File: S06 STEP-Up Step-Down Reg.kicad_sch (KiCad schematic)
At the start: 49 parts, among them Q16 IAUCN04S7L019, Q17 IAUCN04S7L028, Q18 CSD17304Q3, Q19 IAUCN04S7L019, U5 LM51772RHAR

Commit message: Add a PCAL9714 SPI I/O expander for the load-switch enables and faults
New sheet S08 with U11 (PCAL9714, HVQFN-24) on the shared CLOCK/MOSI/MISO
bus. J3.32, which was ENSBC, becomes its chip select nCSIO.

- P0_0-P0_2 drive ENDAQ, ENSBC and ENEXT. J3.34/J3.36 become MCU_ENDAQ
  and MCU_ENEXT, and each reaches its enable only through a DNP 0R link
  (R96-R98). R95 links nCSIO to the expander CS.
- P0_4-P0_6 read the U6/U7/U9 power-good signals, and P0_7 reads U5
  nFLT/nINT.
- REGEN stays a direct J3.12 signal.
- RESET is divided from +12V (R99 100K, R100 40.2K), so the expander
  stays in reset while the 12 V rail is off.
- Pull-ups on CS and INT (R93, R94) and decoupling (C58, C59).

The README gains the port map, the links and the board work. The board
still needs Update PCB from Schematic.

Co-Authored-By: Claude Opus 5.5 <noreply@anthropic.com>
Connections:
- net nFLT: now reaches R40.2, U5.11 (nFLT/nINT)
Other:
- note added: "U5 nFLT/nINT to the I/O expander (S08)"
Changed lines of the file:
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@@
 		)
 	)
+	(text "U5 nFLT/nINT to the I/O expander (S08)"
+		(exclude_from_sim no)
+		(at 266.7 223.52 0)
+		(effects
+			(font
+				(size 1.27 1.27)
+			)
+			(justify left top)
+		)
+	)
 	(text "C"
 		(exclude_from_sim no)
@@
 	(wire
 		(pts
+			(xy 271.78 228.6) (xy 284.48 228.6)
+		)
+		(stroke
+			(width 0)
+			(type default)
+		)
+	)
+	(wire
+		(pts
 			(xy 346.71 59.69) (xy 356.87 59.69)
 		)
@@
 		)
 	)
+	(label "nFLT"
+		(at 140.97 175.26 0)
+		(effects
+			(font
+				(size 1.27 1.27)
+			)
+			(justify left bottom)
+		)
+	)
 	(label "MODE"
 		(at 142.24 160.02 180)
@@
 		)
 	)
+	(label "nFLT"
+		(at 271.78 228.6 180)
+		(effects
+			(font
+				(size 1.27 1.27)
+			)
+			(justify right bottom)
+		)
+	)
 	(label "LDVR1"
 		(at 137.16 95.25 0)
@@
 		)
 	)
+	(hierarchical_label "nFLT"
+		(shape output)
+		(at 284.48 228.6 0)
+		(effects
+			(font
+				(size 1.27 1.27)
+			)
+			(justify left)
+		)
+	)

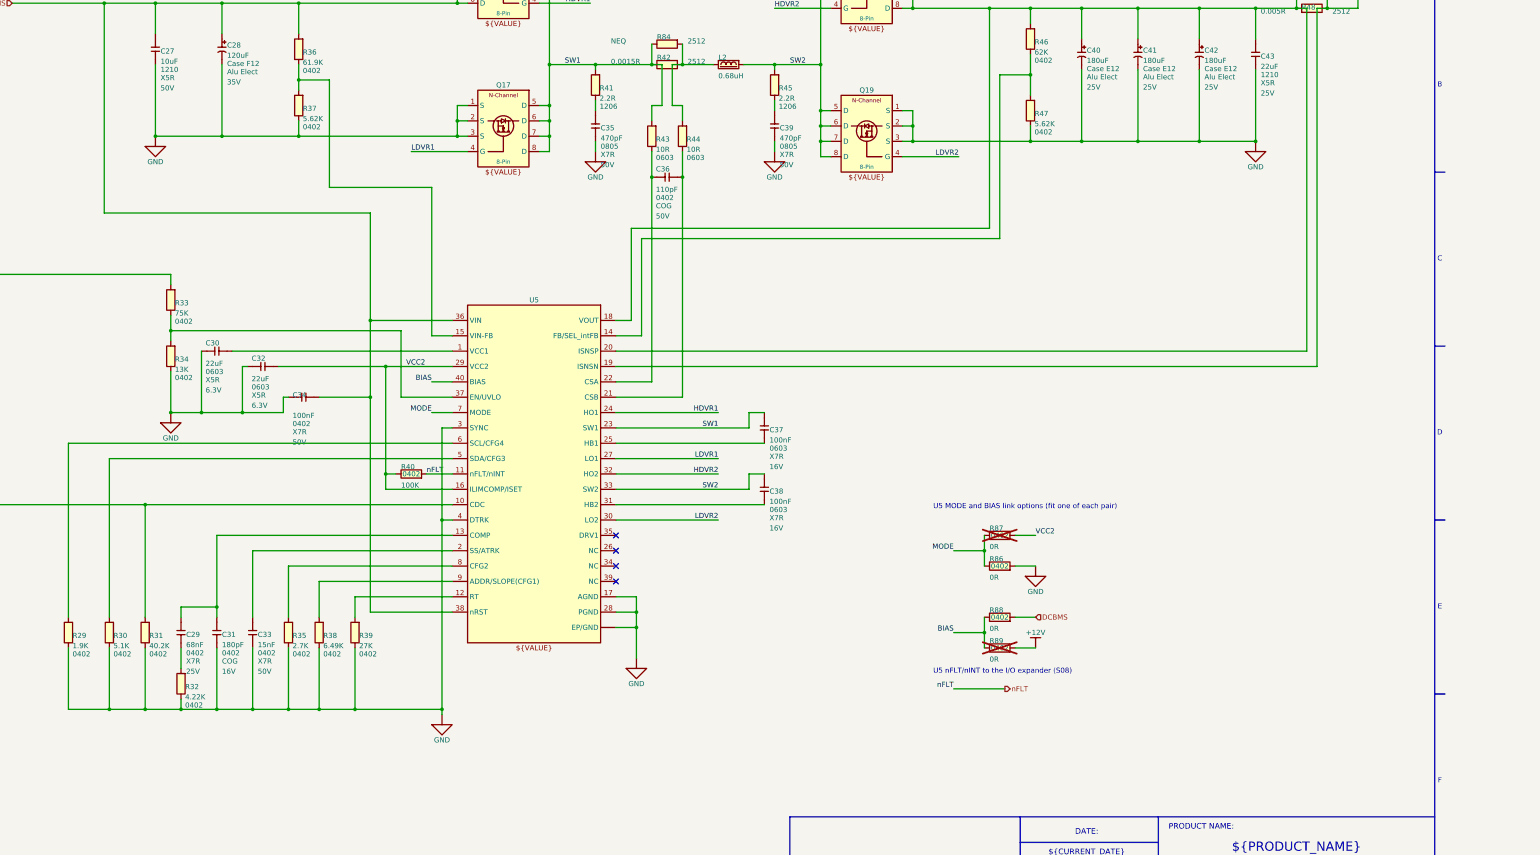
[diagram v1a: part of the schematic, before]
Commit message: BOM consolidation, OVLO divider to 1%, U5 fixes and I2C config option
- Consolidate passives: 1uF 50V to 0603, 100nF to 50V X7R 0402,
  10uF to 50V X7R 1210, 220nF to 0603, 10R to 0402 (100 -> 90 BOM lines)
- TPS22811 OVLO divider 1M/102K 0.1% -> 1M/100K 1% (12.6V min trip)
- U5 LM51772: C30 -> R102 10K to GND (VCC1 disabled), C32 -> 22uF 16V 0805,
  R29 1.9K -> 1.87K to sit inside the CFG4 window
- Add DNP I2C configuration option for U5 (R103-R107) on J3.34/J3.36,
  shared with R97/R98 fallback
- Document all changes in README.md

Co-Authored-By: Claude Opus 5.5 <noreply@anthropic.com>
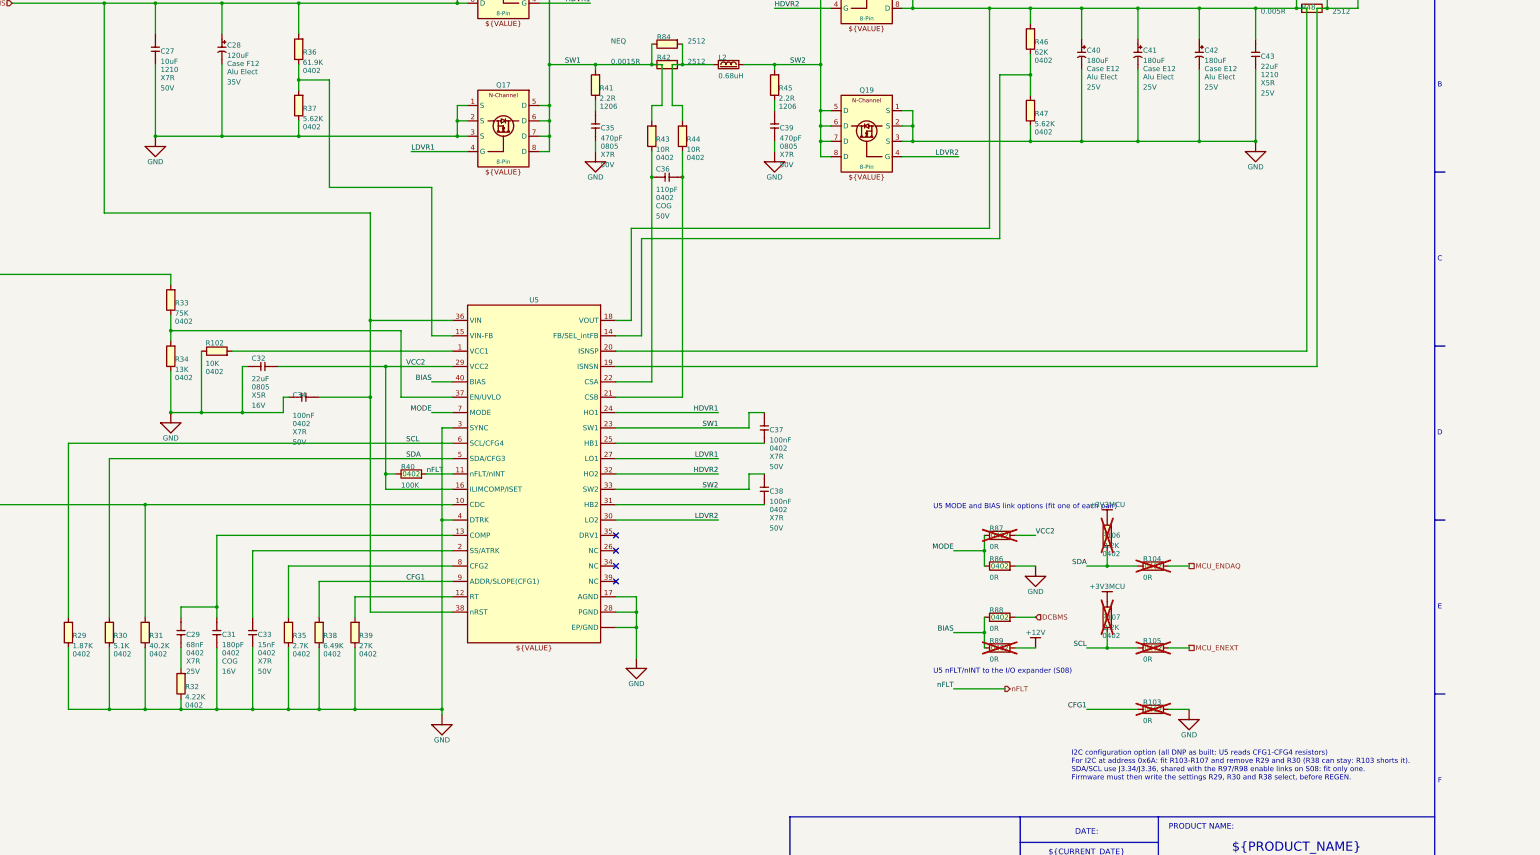
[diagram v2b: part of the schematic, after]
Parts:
- added R103, R104, R105: 0R, Resistor_SMD:R_0402_1005Metric, symbol Lattech Systems:Resistor 0R 0402
- added R106, R107: 2.2K, Resistor_SMD:R_0402_1005Metric, symbol Lattech Systems:Resistor 2.2K 1% 0402
- C27: symbol Lattech Systems:Capacitor 10uF 50V X5R 1210 -> Lattech Systems:Capacitor 10uF 50V X7R 1210; MANUFACTURER (none) -> Murata; MANUFACTURER_PN (none) -> GRM32ER71H106KA12L; MATERIAL X5R -> X7R; PL_SORT_GROUP (none) -> 2.3
- C32: footprint Capacitor_SMD:C_0603_1608Metric -> Capacitor_SMD:C_0805_2012Metric; symbol Lattech Systems:Capacitor 22uF 6.3V X5R 0603 -> Lattech Systems:Capacitor 22uF 16V X5R 0805; ALTIUM_FOOTPRINT 0603 -> 0805; MANUFACTURER ? -> Murata; MANUFACTURER_PN ? -> GRM21BR61C226ME44L; VOLTAGE 6.3V -> 16V
- C34: MANUFACTURER ? -> Yageo; MANUFACTURER_PN ? -> CC0402KPX7R9BB104
- C37, C38: footprint Capacitor_SMD:C_0603_1608Metric -> Capacitor_SMD:C_0402_1005Metric; symbol Lattech Systems:Capacitor 100nF 16V X7R 0603 -> Lattech Systems:Capacitor 100nF 50V X7R 0402; ALTIUM_FOOTPRINT 0603 -> 0402; MANUFACTURER (none) -> Yageo; MANUFACTURER_PN (none) -> CC0402KPX7R9BB104; PL_SORT_GROUP (none) -> 2.3; VOLTAGE 16V -> 50V
- R102: renamed from C30; value 22uF -> 10K; footprint Capacitor_SMD:C_0603_1608Metric -> Resistor_SMD:R_0402_1005Metric; symbol Lattech Systems:Capacitor 22uF 6.3V X5R 0603 -> Lattech Systems:Resistor 10K 1% 0402; ALTIUM_FOOTPRINT 0603 -> 0402; ALTIUM_VALUE 22uF -> 10K; MATERIAL X5R -> (none); VOLTAGE 6.3V -> (none)
- R29: value 1.9K -> 1.87K; symbol Lattech Systems:Resistor 1.9K 1% 0402 -> Lattech Systems:Resistor 1.87K 1% 0402; ALTIUM_VALUE 1.9K -> 1.87K
- R43, R44: footprint Resistor_SMD:R_0603_1608Metric -> Resistor_SMD:R_0402_1005Metric; symbol Lattech Systems:Resistor 10R 1% 0603 -> Lattech Systems:Resistor 10R 1% 0402; ALTIUM_FOOTPRINT 0603 -> 0402
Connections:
- net GND: now also R103.2
- net SDA: now reaches R30.2, U5.5 (SDA/CFG3)
- net SDA: now also R104.1, R106.1
- net SCL: now reaches R29.2, U5.6 (SCL/CFG4)
- net SCL: now also R105.1, R107.1
- net CFG1: now reaches R38.2, U5.9 (ADDR/SLOPE(CFG1))
- net CFG1: now also R103.1
- new net +3V3MCU: R106.2, R107.2
- new net MCU_ENDAQ: R104.2
- new net MCU_ENEXT: R105.2
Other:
- note added: "I2C configuration option (all DNP as built: U5 reads CFG1-CFG4 resistors) For I2C at address 0x6A: fit R103-R107 and remove R29 and R30 (R38 can stay: R103 shorts it). SDA/SCL use J3.34/J3.36, shared with the R97/R98 enable links on S08: fit only one. Firmware must then write the settings R29, R30 and R38 select, before REGEN."

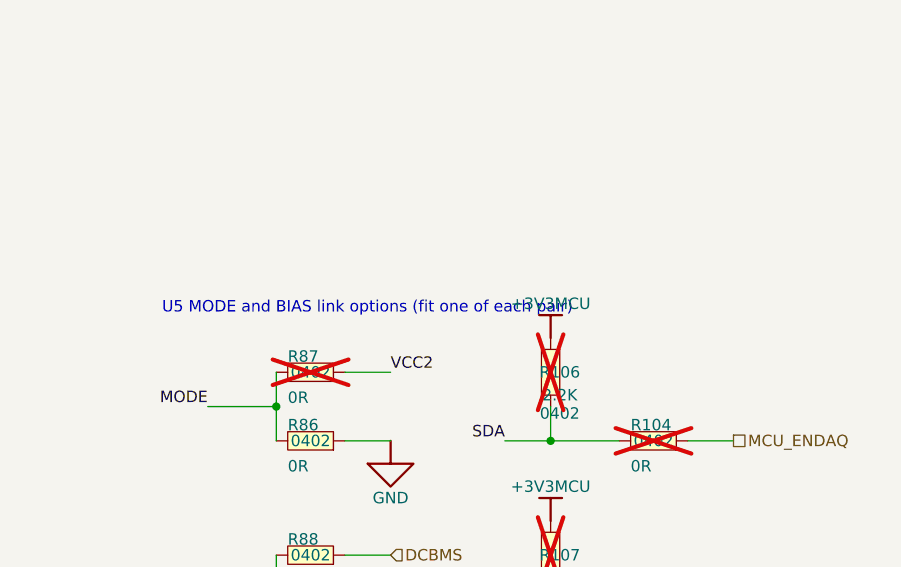
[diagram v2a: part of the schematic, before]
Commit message: Update the PCB from the schematic for the BOM consolidation
Brings in the footprint changes from 2fea505: C11-C14 and C24-C26 to
1210, C8/C9/C55 and C16 to 0603, C32 to 0805, C37/C38 and R43/R44 to
0402, C30 replaced by R102, and the U5 I2C option parts R103-R107.

Q20 moved clear of C42's courtyard, with a few other parts and a via
moved and zones refilled. Minimum hole clearance set to 0.182 mm.

The schematic changes are KiCad reordering items, plus one item moved
on S06.

Co-Authored-By: Claude Opus 5.5 <noreply@anthropic.com>
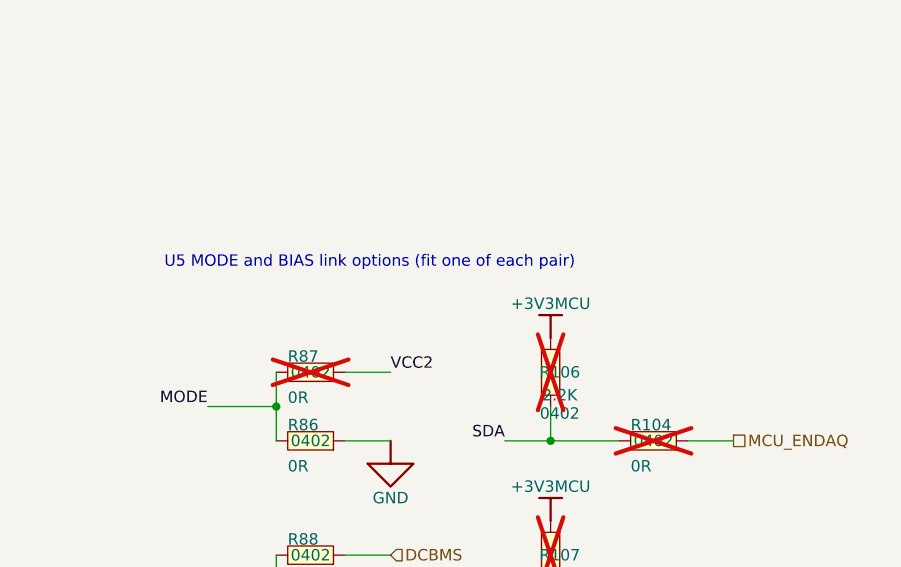
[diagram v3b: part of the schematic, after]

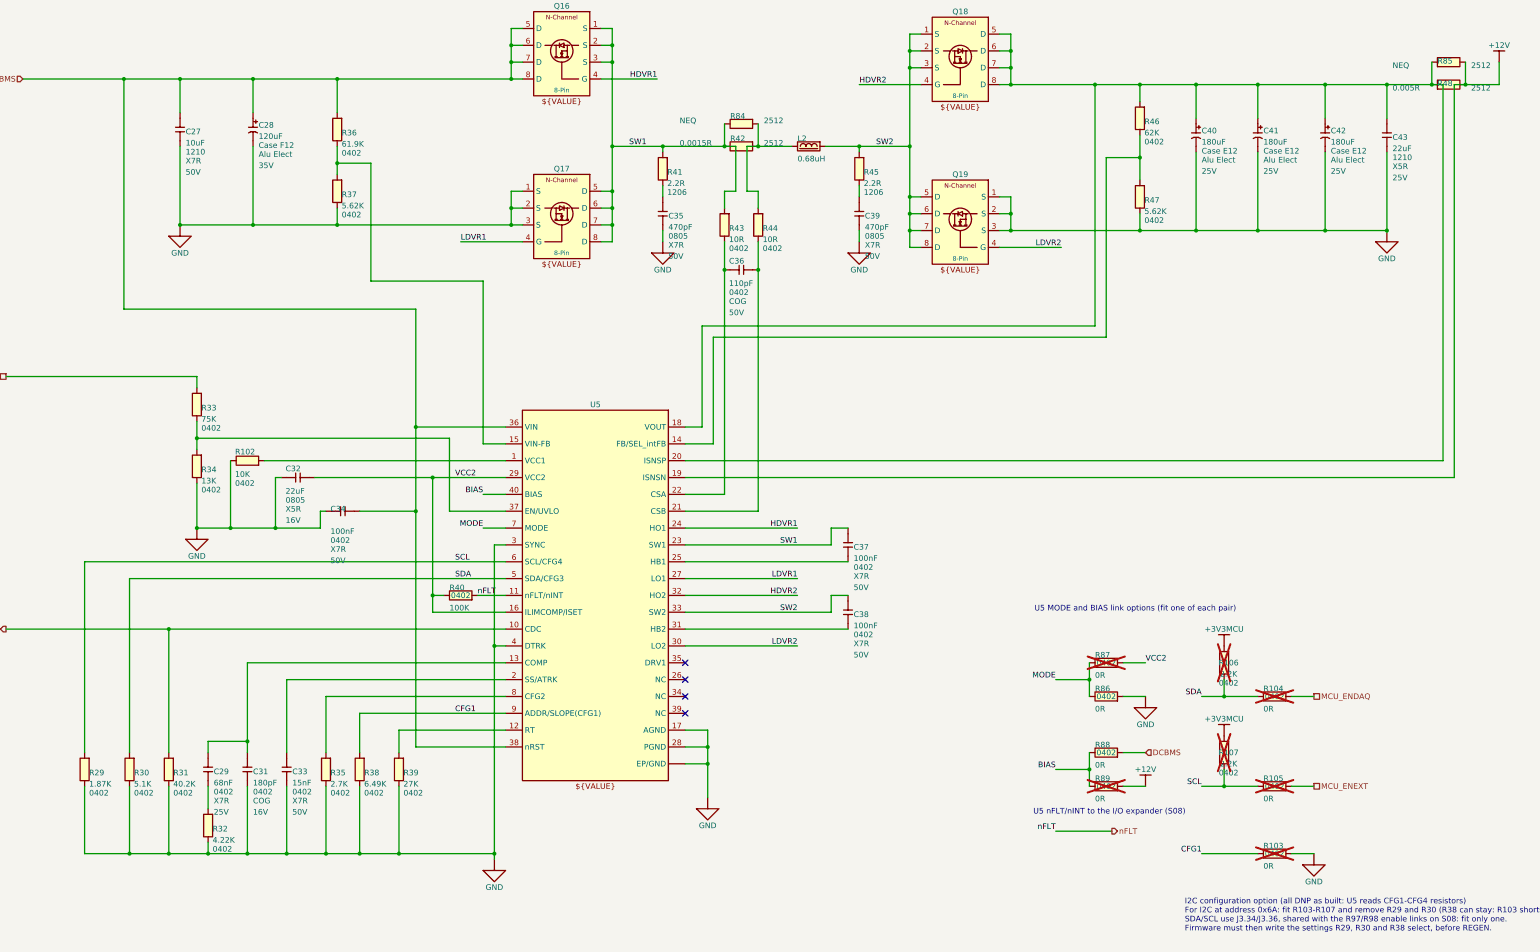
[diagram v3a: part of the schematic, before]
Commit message: Final-revision value changes and standard R/C symbols
Values (schematic and PCB):
- C2 100uF -> 82uF, matching the ordered 35SVPF82M
- C46, C47, C51 (TPS22811 DVDT) 4.7nF -> 1.8nF CC0402KRX7R9BB182 for a
  shorter output ramp
- R24-R27 10R -> 0R; D9, D10 and R36 DNP
- R14 0.01R -> 0.012R PA2512FKF7W0R012E

Symbols:
- All 160 resistors and capacitors now use Device:R, Device:C and
  Device:C_Polarized; the 76 per-value R/C symbols are removed from the
  project library. Connectivity is unchanged (netlist compared).
- Value is now the displayed field instead of ALTIUM_VALUE, which had left
  R1, C39 and R54 showing their old values. ALTIUM_VALUE synced with Value
  on R1, C39, R54, D1, Q1, Q3 and L1.
- Net-(C40-+) is now Net-(U5-ISNSP); renamed on the PCB and in the
  PWR 15A net class pattern.

Co-Authored-By: Claude Opus 5.5 <noreply@anthropic.com>
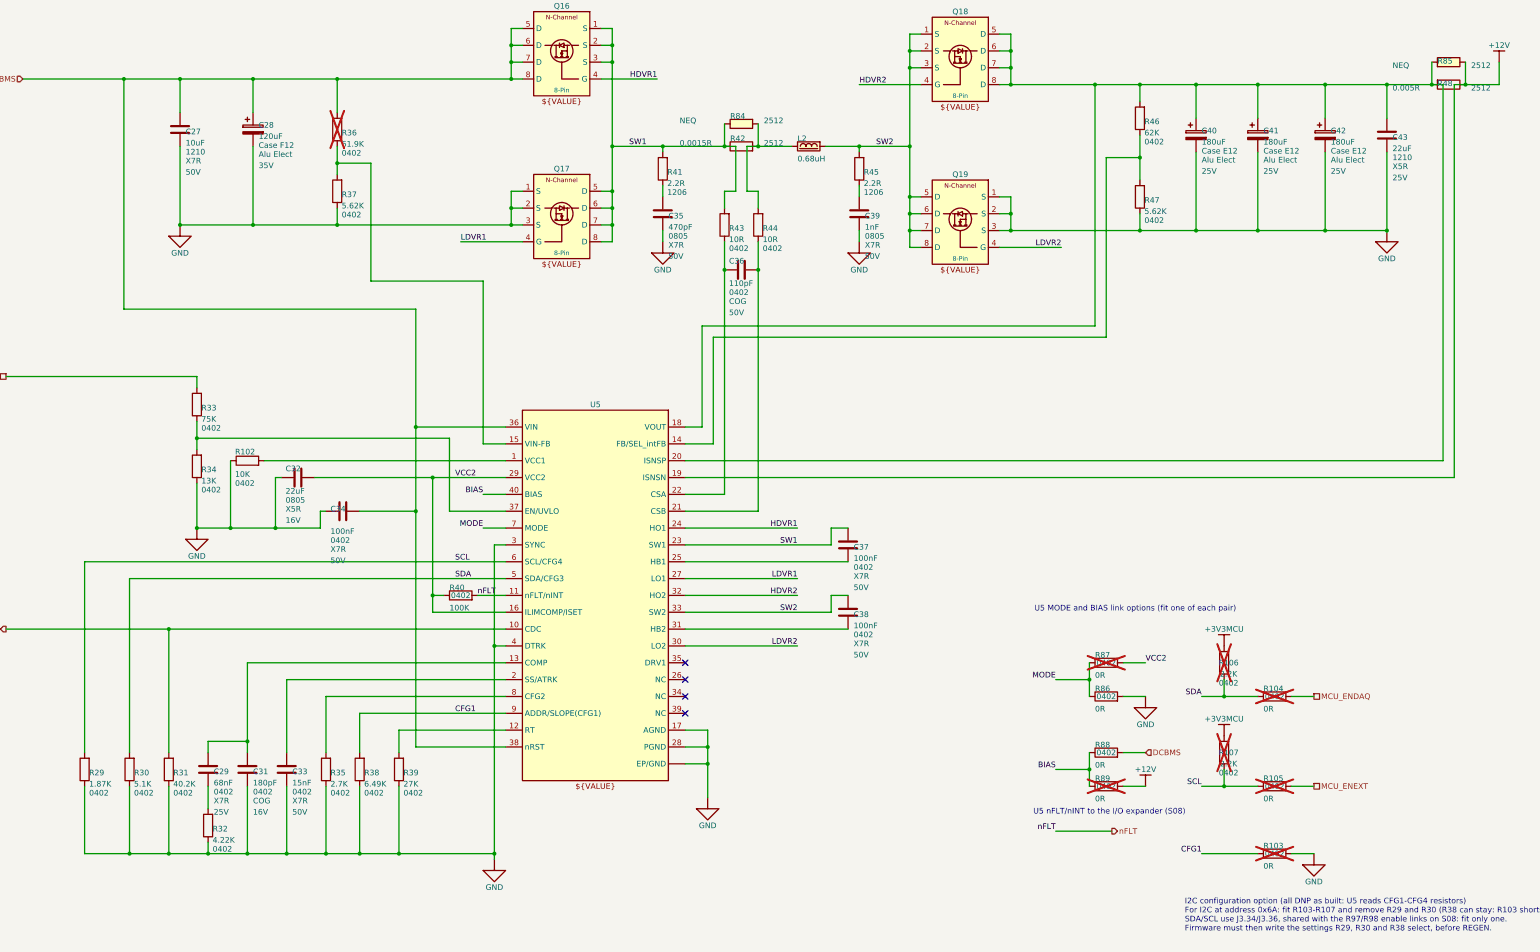
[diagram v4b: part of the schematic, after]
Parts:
- C27: symbol Lattech Systems:Capacitor 10uF 50V X7R 1210 -> Device:C
- C28: symbol Lattech Systems:Capacitor 120uF 35V Alu Elect SVPF Case F12 -> Device:C_Polarized
- C29: symbol Lattech Systems:Capacitor 68nF 25V X7R 0402 -> Device:C
- C31: symbol Lattech Systems:Capacitor 180pF 16V C0G 0402 -> Device:C
- C32: symbol Lattech Systems:Capacitor 22uF 16V X5R 0805 -> Device:C
- C33: symbol Lattech Systems:Capacitor 15nF 50V X7R 0402 -> Device:C
- C34, C37, C38: symbol Lattech Systems:Capacitor 100nF 50V X7R 0402 -> Device:C
- C35: symbol Lattech Systems:Capacitor 470pF 50V X7R 0805 -> Device:C
- C36: symbol Lattech Systems:Capacitor 110pF 50V C0G 0402 -> Device:C
- C39: symbol Lattech Systems:Capacitor 1nF 50V X7R 0805 -> Device:C; ALTIUM_VALUE 470pF -> 1nF
- C40, C41, C42: symbol Lattech Systems:Capacitor 180uF 25V Alu Elect SVPF Case E12 -> Device:C_Polarized
- C43: symbol Lattech Systems:Capacitor 22uF 25V X5R 1210 -> Device:C
- R102: symbol Lattech Systems:Resistor 10K 1% 0402 -> Device:R
- R103, R104, R105, R86, R87, R88, R89: symbol Lattech Systems:Resistor 0R 0402 -> Device:R
- R106, R107: symbol Lattech Systems:Resistor 2.2K 1% 0402 -> Device:R
- R29: symbol Lattech Systems:Resistor 1.87K 1% 0402 -> Device:R
- R30: symbol Lattech Systems:Resistor 5.1K 1% 0402 -> Device:R
- R31: symbol Lattech Systems:Resistor 40.2K 1% 0402 -> Device:R
- R32: symbol Lattech Systems:Resistor 4.22K 1% 0402 -> Device:R
- R33: symbol Lattech Systems:Resistor 75K 1% 0402 -> Device:R
- R34: symbol Lattech Systems:Resistor 13K 1% 0402 -> Device:R
- R35: symbol Lattech Systems:Resistor 2.7K 1% 0402 -> Device:R
- R36: symbol Lattech Systems:Resistor 61.9K 1% 0402 -> Device:R; now not fitted
- R37, R47: symbol Lattech Systems:Resistor 5.62K 1% 0402 -> Device:R
- R38: symbol Lattech Systems:Resistor 6.49K 1% 0402 -> Device:R
- R39: symbol Lattech Systems:Resistor 27K 1% 0402 -> Device:R
- R40: symbol Lattech Systems:Resistor 100K 1% 0402 -> Device:R
- R41, R45: symbol Lattech Systems:Resistor 2.2R 1% 1206 -> Device:R
- R42: symbol Lattech Systems:Resistor 0.0015R 1% 2W 2512 -> Device:R
- R43, R44: symbol Lattech Systems:Resistor 10R 1% 0402 -> Device:R
- R46: symbol Lattech Systems:Resistor 62K 1% 0402 -> Device:R
- R48: symbol Lattech Systems:Resistor 0.005R 1% 3W 2512 -> Device:R
